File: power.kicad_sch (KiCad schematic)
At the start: 22 parts, among them J24 ACT ARMED, J25 PWR IN, J26 ACT DISARMED, J27 ENERGIZE, K1 J115F11C, Q2 NMOS, U35 TLI4971, U36 TLP241A, U37 ADS1110

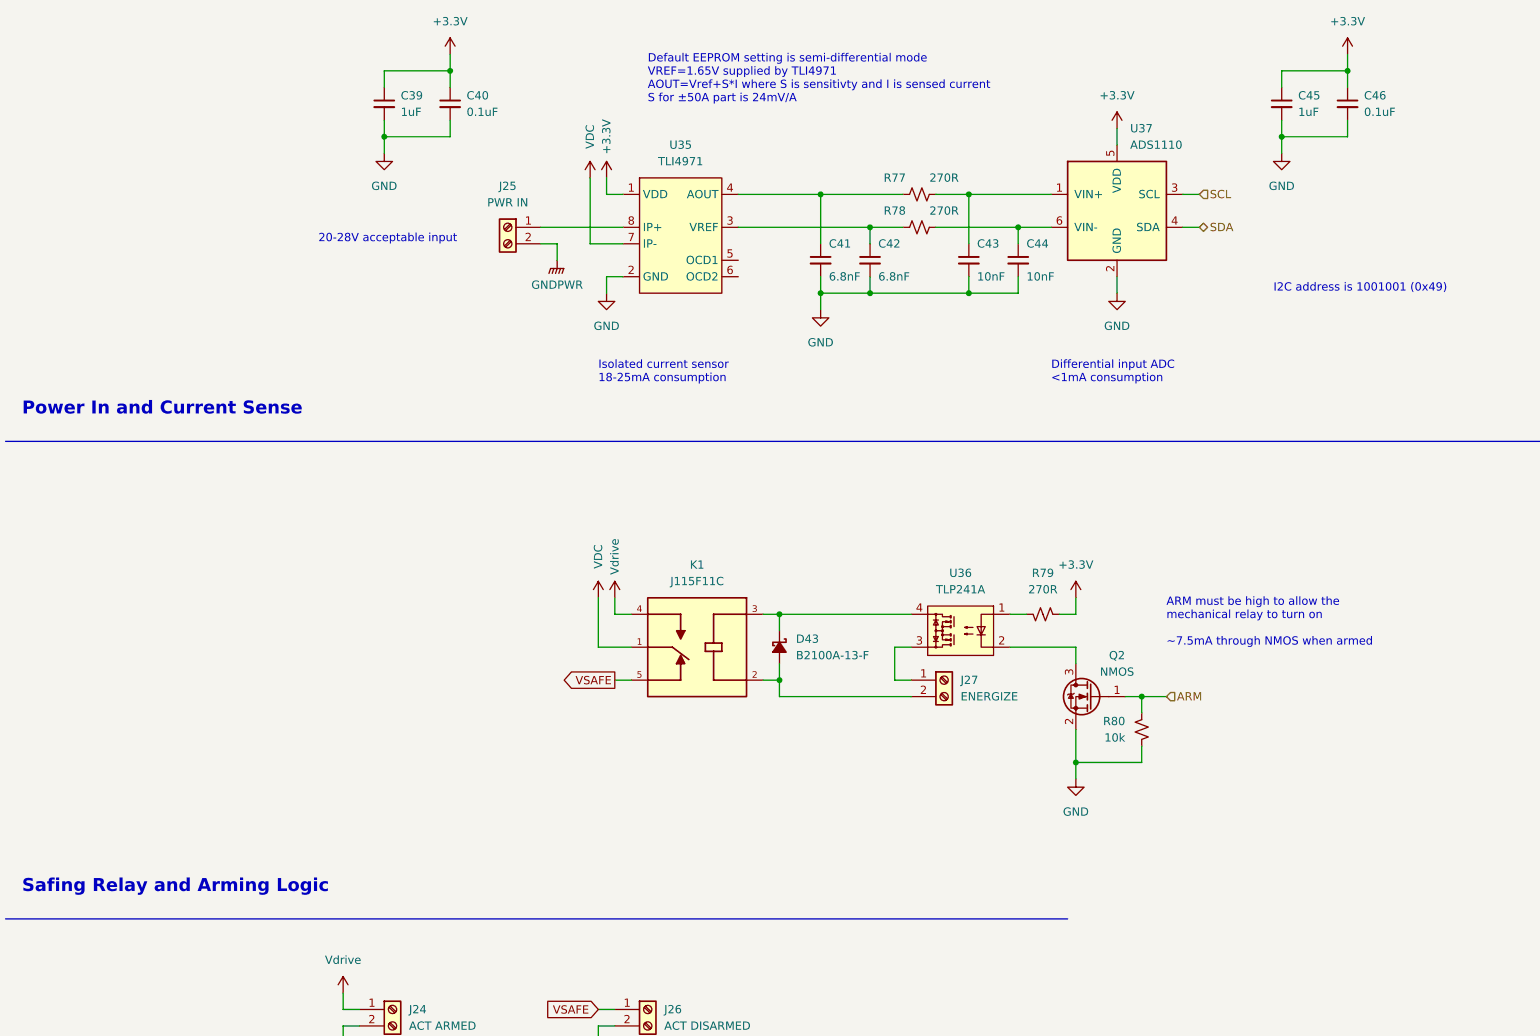
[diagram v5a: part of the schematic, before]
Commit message: Footprints, some part selection, external power outputs
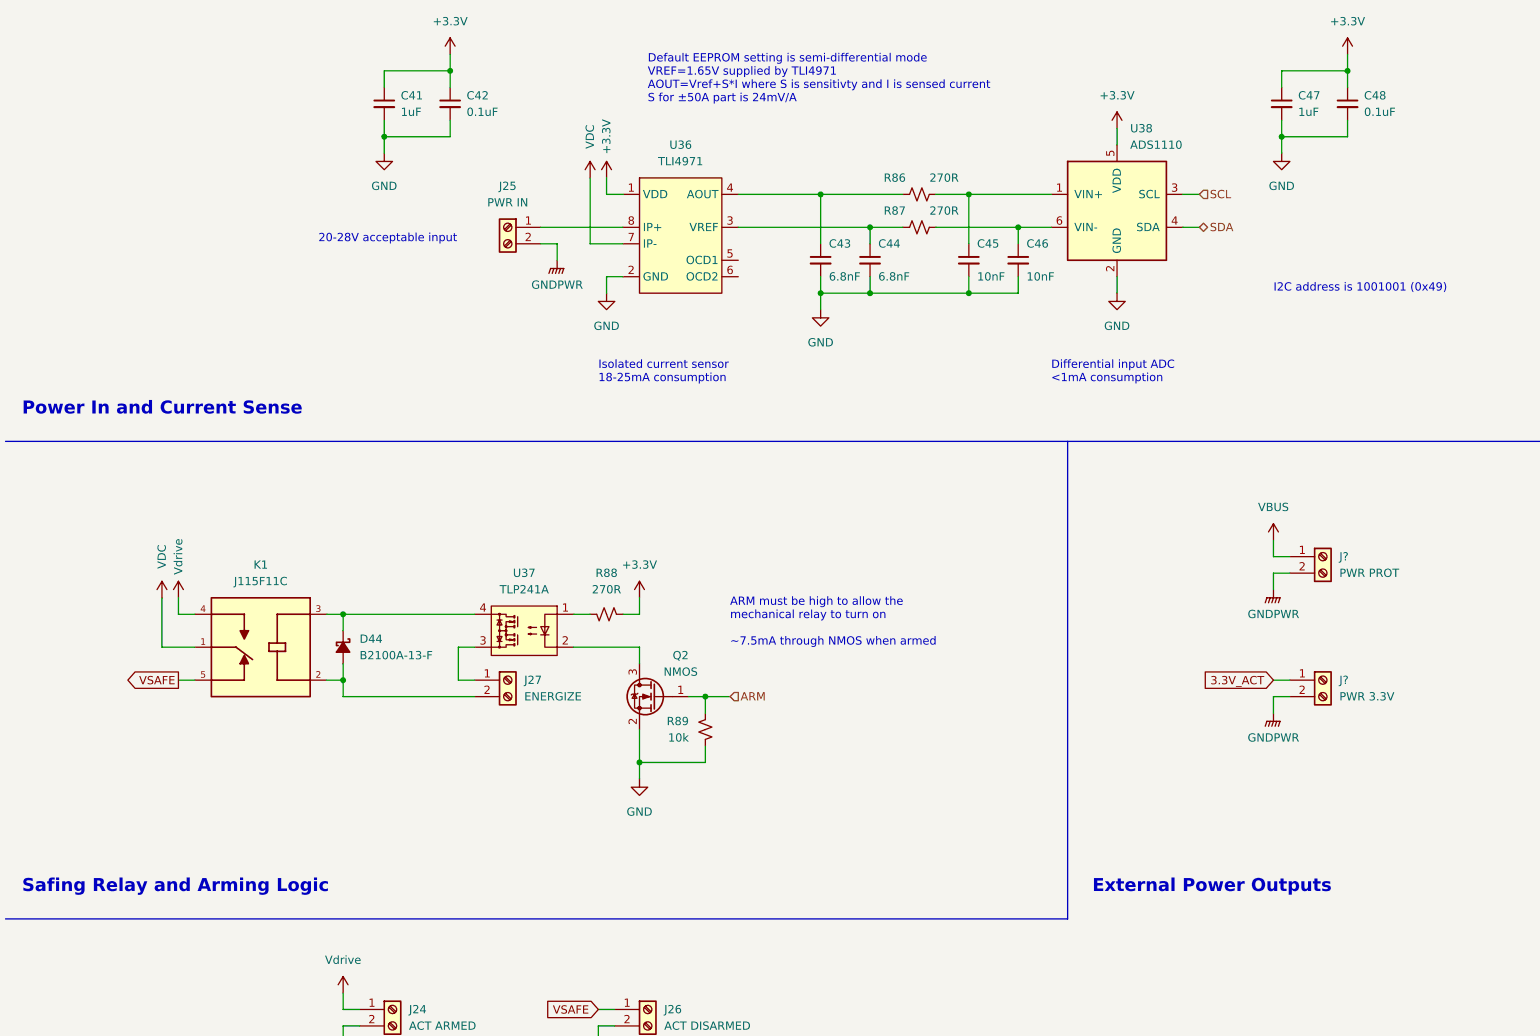
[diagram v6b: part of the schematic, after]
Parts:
- added J?: PWR PROT, TerminalBlock_Phoenix:TerminalBlock_Phoenix_PT-1,5-2-5.0-H_1x02_P5.00mm_Horizontal, symbol Connector:Screw_Terminal_01x02
- added J?: PWR 3.3V, TerminalBlock_Phoenix:TerminalBlock_Phoenix_PT-1,5-2-5.0-H_1x02_P5.00mm_Horizontal, symbol Connector:Screw_Terminal_01x02
- C43: renamed from C41; footprint (none) -> Capacitor_SMD:C_0603_1608Metric
- C44: renamed from C42; footprint (none) -> Capacitor_SMD:C_0603_1608Metric
- C45: renamed from C43; footprint (none) -> Capacitor_SMD:C_0603_1608Metric
- C46: renamed from C44; footprint (none) -> Capacitor_SMD:C_0603_1608Metric
- J25: footprint (none) -> actuation:1773976
- Q2: footprint (none) -> Package_TO_SOT_SMD:SOT-23-3; MPN (none) -> PMV40UN2R
- R86: renamed from R77; footprint (none) -> Resistor_SMD:R_0603_1608Metric
- R87: renamed from R78; footprint (none) -> Resistor_SMD:R_0603_1608Metric
- R89: renamed from R80; footprint (none) -> Resistor_SMD:R_0603_1608Metric
- U37: renamed from U36; footprint actuation:11-5B2S -> actuation:TLP241A
- renumbered C39 to C41, C40 to C42, C45 to C47, C46 to C48, D43 to D44, R79 to R88, U35 to U36, U37 to U38
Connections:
- net GNDPWR: now also J?.2 (Pin_2), J?.2 (Pin_2)
- new net 3.3V_ACT: J?.1 (Pin_1)
- new net VBUS: J?.1 (Pin_1)
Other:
- note added: "External Power Outputs"
- moved on the sheet: D44, J27, K1, Q2, R88, R89, U37

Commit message: Schematic reorganization
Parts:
- added C? (x2): 10uF, Capacitor_SMD:C_0805_2012Metric, symbol Device:C_Small
- added C? (x2): 22uF, Capacitor_SMD:C_1206_3216Metric, symbol Device:C_Small
- added C? (x2): 1uF, Capacitor_SMD:C_0603_1608Metric, symbol Device:C_Small
- added C? (x3): 10uF, Capacitor_SMD:C_1206_3216Metric, symbol Device:C_Small
- added C?: 68nF, Capacitor_SMD:C_0603_1608Metric, symbol Device:C_Small
- added C?: 0.1uF, Capacitor_SMD:C_0603_1608Metric, symbol Device:C_Small
- added C?: 3.3nF, Capacitor_SMD:C_0603_1608Metric, symbol Device:C_Small
- added C?: 6nF, Capacitor_SMD:C_0603_1608Metric, symbol Device:C_Small
- added D?: SMAJ40CA-13-F, Diode_SMD:D_SMA, symbol Device:D_TVS_Filled
- added D?: CTRL PWR, LED_SMD:LED_0603_1608Metric, symbol Device:LED_Small_Filled
- added D?: FB PWR, LED_SMD:LED_0603_1608Metric, symbol Device:LED_Small_Filled
- added L?: 4.7uH, Inductor_SMD:L_Vishay_IHLP-2020, symbol Device:L_Small
- added Q? (x2): SI7220 NMOS, Package_SO:Vishay_PowerPAK_1212-8_Dual, symbol Device:Q_Dual_NMOS_S1G1S2G2D2D2D1D1
- added R?: 510k, Resistor_SMD:R_0603_1608Metric, symbol Device:R_Small_US
- added R? (x2): 10R, Resistor_SMD:R_0603_1608Metric, symbol Device:R_Small_US
- added R?: 5.1k, Resistor_SMD:R_0603_1608Metric, symbol Device:R_Small_US
- added R?: 22.1k, Resistor_SMD:R_0603_1608Metric, symbol Device:R_Small_US
- added R?: 32.4k, Resistor_SMD:R_0603_1608Metric, symbol Device:R_Small_US
- added R?: 69.8k, Resistor_SMD:R_0603_1608Metric, symbol Device:R_Small_US
- added R?: 1.87M, Resistor_SMD:R_0603_1608Metric, symbol Device:R_Small_US
- added R? (x2): 470R, Resistor_SMD:R_0603_1608Metric, symbol Device:R_Small_US
- added R?: 9.31k, Resistor_SMD:R_0603_1608Metric, symbol Device:R_Small_US
- added R?: 200k, Resistor_SMD:R_0603_1608Metric, symbol Device:R_Small_US
- added U?: LP5912-3.3DRV, Package_SON:WSON-6-1EP_2x2mm_P0.65mm_EP1x1.6mm_ThermalVias, symbol Regulator_Linear:LP5912-3.3DRV
- added U?: AP64350, Package_SO:SOIC-8-1EP_3.9x4.9mm_P1.27mm_EP2.62x3.51mm, symbol actuation:AP64350
- added U?: LTC4367, Package_DFN_QFN:DFN-8-1EP_3x3mm_P0.5mm_EP1.65x2.38mm, symbol interface:LTC4367
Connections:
- net +3.3V: now also C?.1, C?.1, R?.1, U?.1 (OUT)
- net 3.3V_ACT: now also C?.1, C?.1, L?.2, R?.1, R?.1
- net GND: now also C?.2, C?.2, C?.2, C?.2, D?.1 (K), U?.5 (GND), U?.7 (EP)
- net GNDPWR: now also C?.2, C?.2, C?.2, C?.2, C?.2, C?.2, C?.2, C?.2, D?.1 (A1), D?.1 (K), R?.1, R?.2, R?.2, U?.4 (GND), U?.7 (GND), U?.9 (EPAD), U?.9 (PAD)
- net VBUS: now also C?.1, C?.1, C?.1, Q?.5 (D), U?.2 (VIN), U?.3 (EN), U?.7 (VOUT)
- net VDC: now also D?.2 (A2), Q?.6 (D), R?.2, R?.2, U?.1 (VIN)
- new net: Q?.1 (S), Q?.3 (S)
- new net: Q?.2 (G), R?.1
- new net: R?.1, U?.2 (UV), U?.5 (~{SHDN})
- new net: R?.1, R?.2, R?.2, U?.8 (GATE)
- new net: C?.1, R?.2 (x2)
- new net: R?.1, R?.2, U?.5 (FB)
- new net: R?.1, R?.2, U?.3 (OV)
- new net: C?.1, R?.1, U?.6 (COMP)
- new net: C?.1, U?.1 (BST)
- new net: C?.2, L?.1, U?.8 (SW)
- new net: D?.2 (A), R?.2 (x2)
- new net: R?.1, U?.4 (RT/CLK)
- new net: Q?.4 (G), R?.1
- new net +5V: C?.1, C?.1, U?.4 (EN), U?.6 (IN)
- no-connect marks 0 -> 2
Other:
- note added: "200k configures 500kHz switching"
- note added: "3.3V 500mA LDO"
- note added: "64.5V TVS clamp (to clip inductive switching transients)"
- note added: "Buck converter for hot-side"
- note added: "Cold-side Power Supply"
- note added: "Hot-side Feedback Power Supply"
- note added: "Hot-side Power In and Current Sense"
- note added: "Hot-side Safing Relay and Arming Logic"
- note added: "Input voltage 3.8-40V (has UVLO), 3.5A output >70% efficient at 24V"
- note added: "Overvoltage/reverse voltage protection"
- note added: "Reverse voltage protection (-40V) No undervoltage cutoff Overvoltage cutoff 0.5/(32.4/(1870+32.4)) = 29.36 V Protection up to 60V"
- note added: "VBUS is a protected version of the 20-28V"
- note added: "VDC comes directly from the battery (20-28V)"
- note removed: "Power In and Current Sense"
- note removed: "Safing Relay and Arming Logic"
- moved on the sheet: C41, C42, C43, C44, C45, C46, C47, C48, D44, J24, J25, J26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
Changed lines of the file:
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@@
 (kicad_sch (version 20211123) (generator eeschema)
-  (paper "A4")
+  (paper "User" 370.002 235.001)

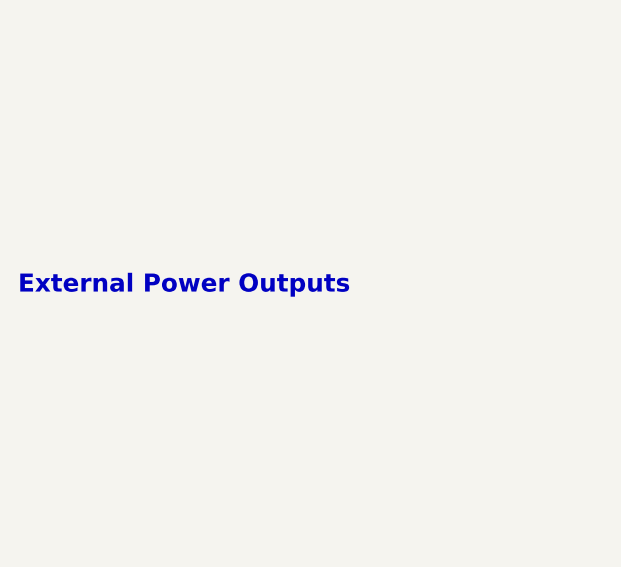
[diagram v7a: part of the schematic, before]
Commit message: TVS diodes for ESD protection on inputs
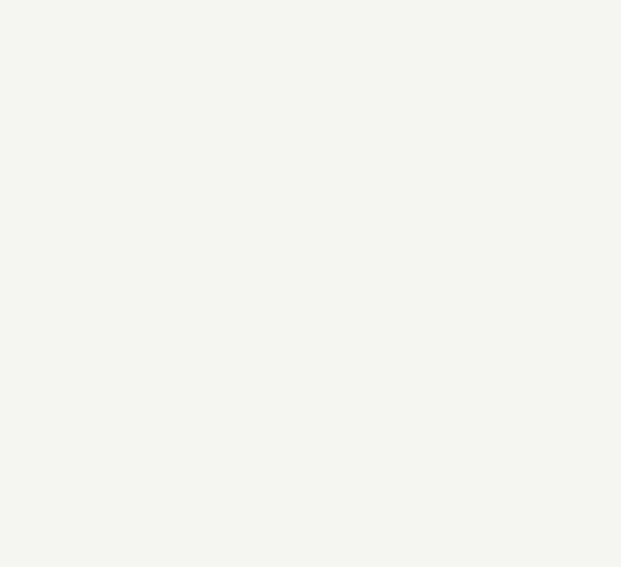
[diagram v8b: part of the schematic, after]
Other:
- note removed: "External Power Outputs"
